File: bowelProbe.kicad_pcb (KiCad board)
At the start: 2 copper layers, 119.8 x 64.8 mm, 53 parts, among them J10 Conn_01x01, J11 Conn_01x01, J12 Conn_01x01, J13 Conn_01x01, J2 Conn_01x01, J3 Conn_01x01, J4 Conn_01x01, J5 Conn_01x01, J6 Conn_01x01, J7 Conn_01x01, J8 Conn_01x01, J9 Conn_01x01, U1 MAX038CPP, U2 OPA2134PA, U3 MCP6002-E/P, U4 TL072ACP

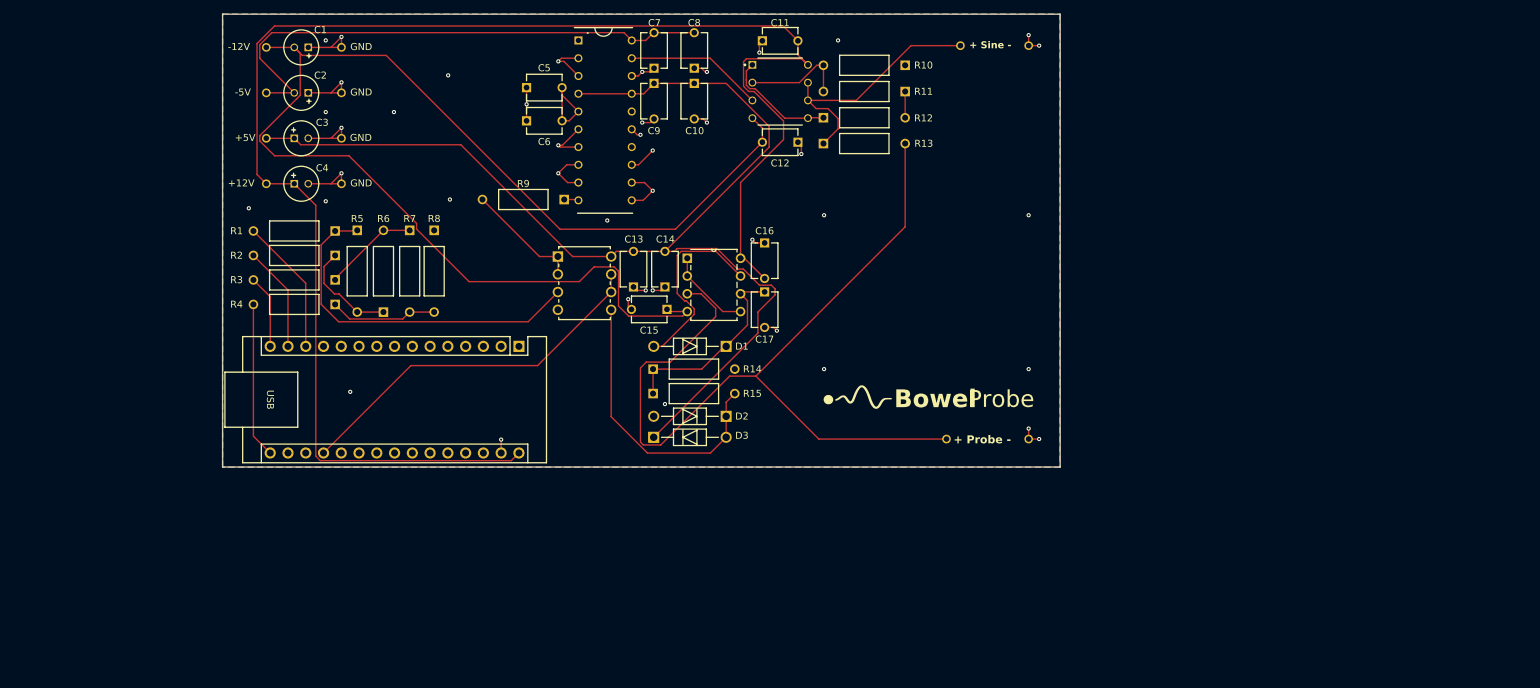
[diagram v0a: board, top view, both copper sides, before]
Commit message: Finished Electronic Schematic, Awaiting Finalizations and Review
Added many symbols, footprints, and 3d models. Organized design into functional blocks.

Still need finalized plans and footprints for "demo".

Next Steps:
 - Finalize "demo" subciruit
 - Review schematic

- Move on to layout

- Make code for full device operation
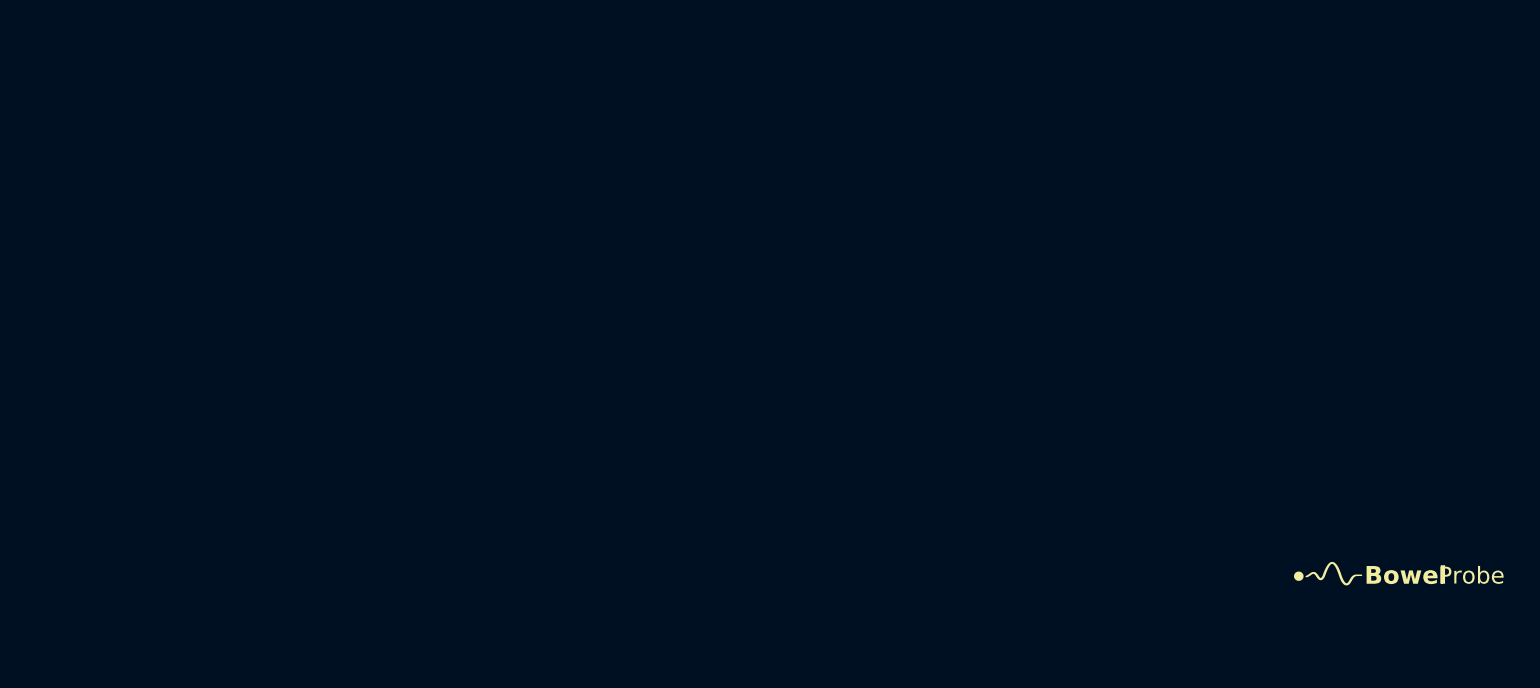
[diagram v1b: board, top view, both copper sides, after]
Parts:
- removed A1: Arduino_Nano_v2.x, Module:Arduino_Nano
- removed C1, C2, C3, C4: 10u, BowelProbe:Capacitor-10u
- removed C10, C14, C8: 1u, BowelProbe:Capacitor-10n
- removed C11, C12, C13, C15, C16, C17: 0.1u, BowelProbe:Capacitor-10n
- removed C5, C6: 10n, BowelProbe:Capacitor-10n
- removed C7, C9: 1n, BowelProbe:Capacitor-10n
- removed D1, D2, D3: DIOAD1036W78L470D235, BowelProbe:1N5817
- removed J10, J11: Conn_01x01, BowelProbe:CT3149-5
- removed J12, J13, J3, J4, J6, J8: Conn_01x01, BowelProbe:CT3149-0
- removed J2, J5, J7, J9: Conn_01x01, BowelProbe:CT3149-2
- removed R1, R11, R12, R2, R3, R4, R8: 20k, BowelProbe:Resistor-20k
- removed R10, R5, R6, R7: 10k, BowelProbe:Resistor-20k
- removed R13: 100, BowelProbe:Resistor-20k
- removed R14: 300k, BowelProbe:Resistor-20k
- removed R15: 1k, BowelProbe:Resistor-20k
- removed R9: 25k, BowelProbe:Resistor-20k
- removed U1: MAX038CPP, BowelProbe:MAX038CPP
- removed U2: OPA2134PA, BowelProbe:DIP794W45P254L959H508Q8
- removed U3: MCP6002-E/P, BowelProbe:PDIP8_300MC_MCH
- removed U4: TL072ACP, BowelProbe:P8
- moved G*** 71.8 mm to (249.1, 115.0)
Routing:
- net Net-(A1-VIN): track 225.7 -> 0.00 mm
- net Net-(J5-Pin_1): track 186.9 -> 0.00 mm
- net Net-(D3-K): track 165.5 -> 0.00 mm
- net Net-(J10-Pin_1): track 124.7 -> 0.00 mm
- net GND: track 101.9 -> 0.00 mm, vias 42 -> 0
- net Net-(J2-Pin_1): track 76.7 -> 0.00 mm
- net Net-(A1-A0): track 53.2 -> 0.00 mm
- net Net-(R1-Pad1): track 51.1 -> 0.00 mm
- net Net-(D2-K): track 41.6 -> 0.00 mm
- net Net-(J12-Pin_1): track 37.4 -> 0.00 mm
- net Net-(D1-K): track 28.0 -> 0.00 mm
- net Net-(D1-A): track 28.0 -> 0.00 mm
- net Net-(A1-D13): track 22.2 -> 0.00 mm
- net Net-(U1-OUT): track 19.7 -> 0.00 mm
- net Net-(A1-D10): track 19.6 -> 0.00 mm
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- removed copper zone on B.Cu, net GND
- removed copper zone on F.Cu, net GND
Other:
- board outline removed
- board text removed: "+ Probe -"
- board text removed: "+ Sine -"
- board text removed: "+12V"
- board text removed: "+5V"
- board text removed: "-12V"
- board text removed: "-5V"
- board text removed: "GND"

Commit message: LTspice Source Scripting
Created python script to model sine wave generator (replacement model for chip AD9833 w/o spice model). Additionally began initial pcb placement.
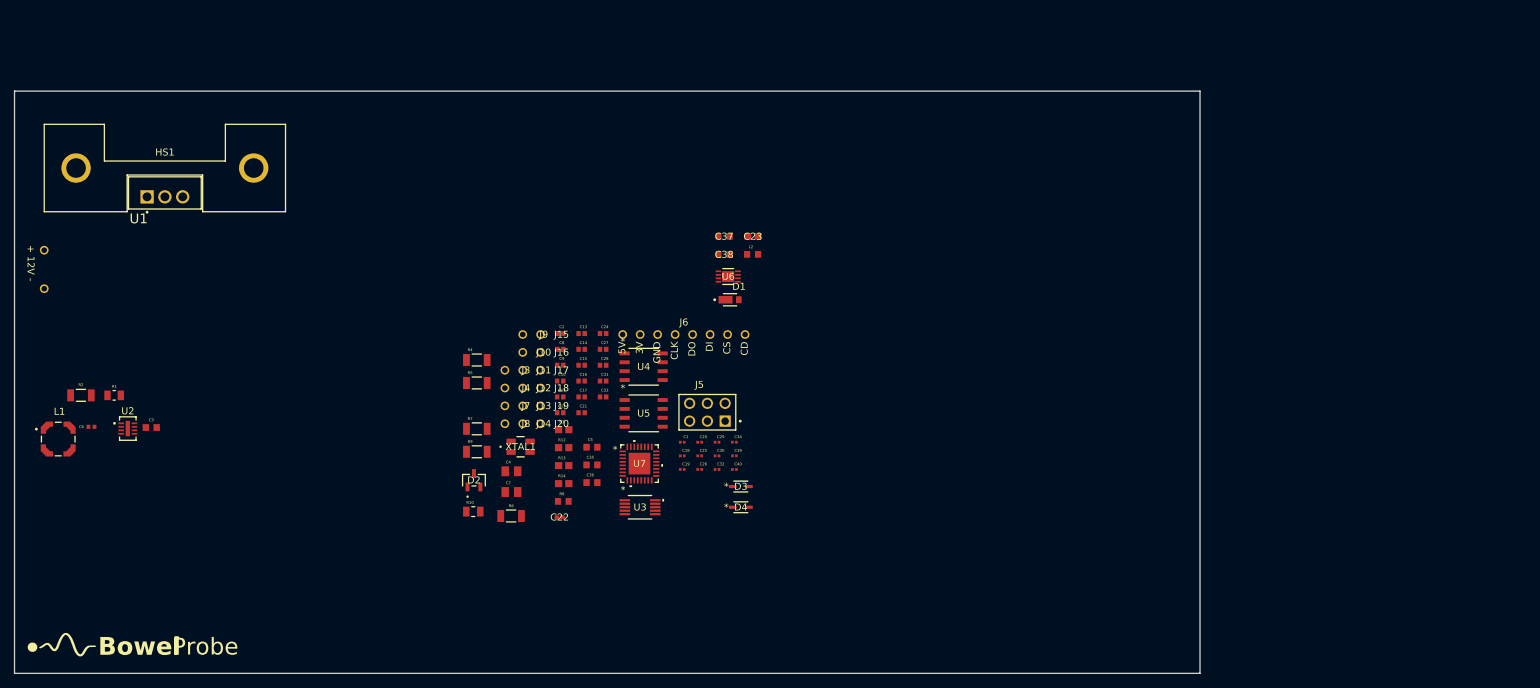
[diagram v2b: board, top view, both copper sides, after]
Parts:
- added C1: 0.1u, BowelProbe:Cap0.1uF, F.Cu at (156.7, 95.7)
- added C10: 10u, BowelProbe:Cap10uF, F.Cu at (139.3, 87.0)
- added C11: 10u, BowelProbe:Cap10uF, F.Cu at (139.3, 89.2)
- added C12: 10u, BowelProbe:Cap10uF, F.Cu at (139.3, 91.5)
- added C13: 10u, BowelProbe:Cap10uF, F.Cu at (142.3, 80.2)
- added C14: 10u, BowelProbe:Cap10uF, F.Cu at (142.3, 82.4)
- added C15: 10u, BowelProbe:Cap10uF, F.Cu at (142.3, 84.7)
- added C16: 10u, BowelProbe:Cap10uF, F.Cu at (142.3, 87.0)
- added C17: 10u, BowelProbe:Cap10uF, F.Cu at (142.3, 89.2)
- added C18: 0.1u, BowelProbe:Cap0.1uF, F.Cu at (156.7, 97.6)
- added C19: 0.1u, BowelProbe:Cap0.1uF, F.Cu at (156.7, 99.6)
- added C2: 10u, BowelProbe:Cap10uF, F.Cu at (139.3, 80.2)
- added C20: 0.1u, BowelProbe:Cap0.1uF, F.Cu at (159.2, 95.7)
- added C21: 10u, BowelProbe:Cap10uF, F.Cu at (142.3, 91.5)
- added C22: 2.2n, BowelProbe:Cap2.2nF, F.Cu at (139.2, 106.4)
- added C23: 1n, BowelProbe:Cap1nF, F.Cu at (166.8, 66.3)
- added C24: 10u, BowelProbe:Cap10uF, F.Cu at (145.4, 80.2)
- added C25: 0.1u, BowelProbe:Cap0.1uF, F.Cu at (159.2, 97.6)
- added C26: 0.1u, BowelProbe:Cap0.1uF, F.Cu at (159.2, 99.6)
- added C27: 10u, BowelProbe:Cap10uF, F.Cu at (145.4, 82.4)
- added C28: 10u, BowelProbe:Cap10uF, F.Cu at (145.4, 84.7)
- added C29: 0.1u, BowelProbe:Cap0.1uF, F.Cu at (161.7, 95.7)
- added C3: 1u, BowelProbe:Cap1uF, F.Cu at (80.8, 93.6)
- added C30: 0.1u, BowelProbe:Cap0.1uF, F.Cu at (161.7, 97.6)
- added C31: 10u, BowelProbe:Cap10uF, F.Cu at (145.4, 87.0)
- added C32: 0.1u, BowelProbe:Cap0.1uF, F.Cu at (161.7, 99.6)
- added C33: 10u, BowelProbe:Cap10uF, F.Cu at (145.4, 89.2)
- added C34: 0.1u, BowelProbe:Cap0.1uF, F.Cu at (164.2, 95.7)
- added C35: 1u, BowelProbe:Cap1uF, F.Cu at (143.8, 98.9)
- added C36: 1u, BowelProbe:Cap1uF, F.Cu at (143.8, 101.5)
- added C37: 18p, BowelProbe:Cap18pF, F.Cu at (162.7, 66.3)
- added C38: 18p, BowelProbe:Cap18pF, F.Cu at (162.7, 68.9)
- added C39: 0.1u, BowelProbe:Cap0.1uF, F.Cu at (164.2, 97.6)
- added C4: 4.7u, BowelProbe:Cap4.7uF, F.Cu at (132.3, 99.9)
- added C40: 0.1u, BowelProbe:Cap0.1uF, F.Cu at (164.2, 99.6)
- added C5: 1u, BowelProbe:Cap1uF, F.Cu at (143.8, 96.4)
- added C6: 4.7p, BowelProbe:Cap4.7pF, F.Cu at (72.2, 93.5)
- added C7: 4.7u, BowelProbe:Cap4.7uF, F.Cu at (132.3, 102.8)
- added C8: 10u, BowelProbe:Cap10uF, F.Cu at (139.3, 82.4)
- added C9: 10u, BowelProbe:Cap10uF, F.Cu at (139.3, 84.7)
- added D1: SchottkyDiode, BowelProbe:SchottkyDiode, F.Cu at (163.6, 75.3)
- added D2: DiodeLowLeak, BowelProbe:DiodeLowLeak, F.Cu at (126.9, 101.1)
- added D3: DiodeClamper, BowelProbe:DiodeClamper, F.Cu at (165.1, 102.0)
- added D4: DiodeClamper, BowelProbe:DiodeClamper, F.Cu at (165.1, 105.0)
- added HS1: Heatsink, BowelProbe:Heatsink, F.Cu at (82.8, 56.5)
- added J1: Conn_01x01, BowelProbe:CT3149-0, F.Cu at (65.5, 73.8)
- added J10: Conn_01x01, BowelProbe:CT3149-0, F.Cu at (133.9, 82.9)
- added J11: Conn_01x01, BowelProbe:CT3149-0, F.Cu at (133.9, 85.4)
- added J12: Conn_01x01, BowelProbe:CT3149-0, F.Cu at (133.9, 88.0)
- added J13: Conn_01x01, BowelProbe:CT3149-0, F.Cu at (133.9, 90.5)
- added J14: Conn_01x01, BowelProbe:CT3149-0, F.Cu at (133.9, 93.1)
- added J15: Conn_01x01, BowelProbe:CT3149-0, F.Cu at (136.5, 80.3)
- added J16: Conn_01x01, BowelProbe:CT3149-0, F.Cu at (136.5, 82.9)
- added J17: Conn_01x01, BowelProbe:CT3149-0, F.Cu at (136.5, 85.4)
- added J18: Conn_01x01, BowelProbe:CT3149-0, F.Cu at (136.5, 88.0)
- added J19: Conn_01x01, BowelProbe:CT3149-0, F.Cu at (136.5, 90.5)
- added J2: Conn_01x01, BowelProbe:CT3149-2, F.Cu at (65.5, 68.2)
- added J20: Conn_01x01, BowelProbe:CT3149-0, F.Cu at (136.5, 93.1)
- added J3: Conn_01x01, BowelProbe:CT3149-5, F.Cu at (131.4, 85.4)
- added J4: Conn_01x01, BowelProbe:CT3149-5, F.Cu at (131.4, 88.0)
- added J5: Conn_02x03_Odd_Even, BowelProbe:Dupont2x3, F.Cu at (160.3, 91.4)
- added J6: Conn_01x08, BowelProbe:microSD, F.Cu at (157.0, 80.3)
- added J7: Conn_01x01, BowelProbe:CT3149-0, F.Cu at (131.4, 90.5)
- added J8: Conn_01x01, BowelProbe:CT3149-0, F.Cu at (131.4, 93.1)
- added J9: Conn_01x01, BowelProbe:CT3149-0, F.Cu at (133.9, 80.3)
- added L1: LPD5030-472MRC, BowelProbe:InductorCoupled, F.Cu at (67.5, 95.2)
- added L2: 10u, BowelProbe:Inductor10uH, F.Cu at (166.8, 68.8)
- added R1: 71.5k, BowelProbe:Resistor71.5k, F.Cu at (75.5, 89.0)
- added R10: 1k, BowelProbe:Resistor1k, F.Cu at (126.8, 105.6)
- added R12: 10k, BowelProbe:Resistor10k, F.Cu at (139.8, 96.5)
- added R13: 10k, BowelProbe:Resistor10k, F.Cu at (139.8, 99.0)
- added R14: 10k, BowelProbe:Resistor10k, F.Cu at (139.8, 101.6)
- added R2: 1M, BowelProbe:Resistor1M, F.Cu at (70.8, 89.0)
- added R3: 10k, BowelProbe:Resistor10k, F.Cu at (139.8, 93.9)
- added R4: 6.8k, BowelProbe:Resistor6.8k, F.Cu at (127.3, 83.9)
- added R5: 6.8k, BowelProbe:Resistor6.8k, F.Cu at (127.3, 87.2)
- added R6: 30k, BowelProbe:Resistor30k, F.Cu at (132.2, 106.2)
- added R7: 1.8k, BowelProbe:Resistor1.8k, F.Cu at (127.3, 93.8)
- added R8: 100, BowelProbe:Resistor100, F.Cu at (139.7, 104.2)
- added R9: 300k, BowelProbe:Resistor300k, F.Cu at (127.3, 97.1)
- added U1: L7805CV, BowelProbe:L7805CV, F.Cu at (80.2, 60.6)
- added U2: LT8330, BowelProbe:LT8330, F.Cu at (77.5, 93.8)
- added U3: AD9833BRMZ, BowelProbe:AD9833, F.Cu at (150.7, 105.0)
- added U4: OPA2134UA/2K5, BowelProbe:OPA2134smd, F.Cu at (151.2, 84.9)
- added U5: TL072ACDR, BowelProbe:TL072smd, F.Cu at (151.2, 91.6)
- added U6: MCP6002-E/MC, BowelProbe:MCP6002smd, F.Cu at (163.3, 72.0)
- added U7: ATmega328P, BowelProbe:ATmega328P, F.Cu at (150.6, 98.8)
- added XTAL1: TSX-3225 16.0000MF09Z-AC3, BowelProbe:Crystal16MHz, F.Cu at (133.6, 96.4)
- moved G*** 181.3 mm to (68.1, 125.2)
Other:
- board outline added: 169.5 x 83.2 mm
- board text added: "+ 12V -"

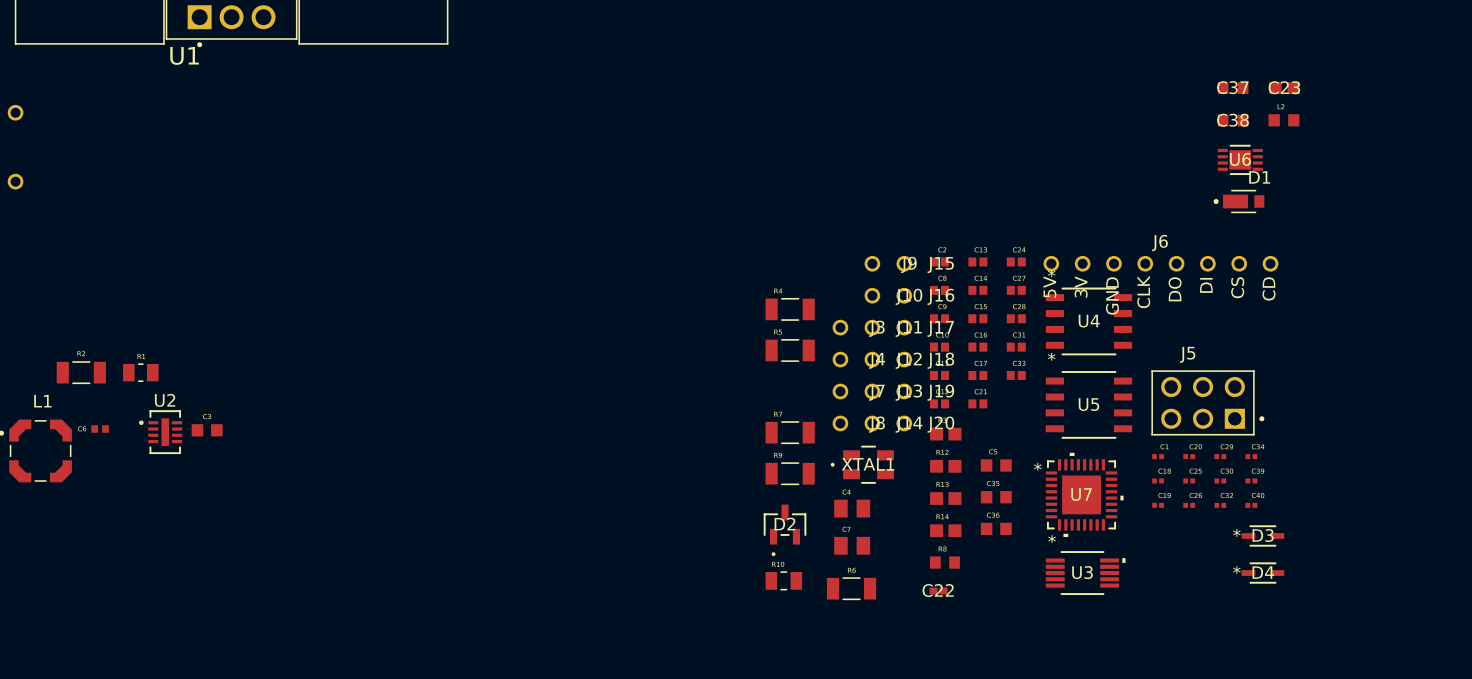
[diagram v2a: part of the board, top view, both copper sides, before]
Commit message: KiCad Updates
Added buffer after wave AD9833 sine generation and coupling capacitor (as simulated in LTspice) to address loading on filter stage. Added symbol, footprint, 3D model, and spice model in corresponding folders.

Updated BOM with this new part and updated PCB layout with buffer parts.
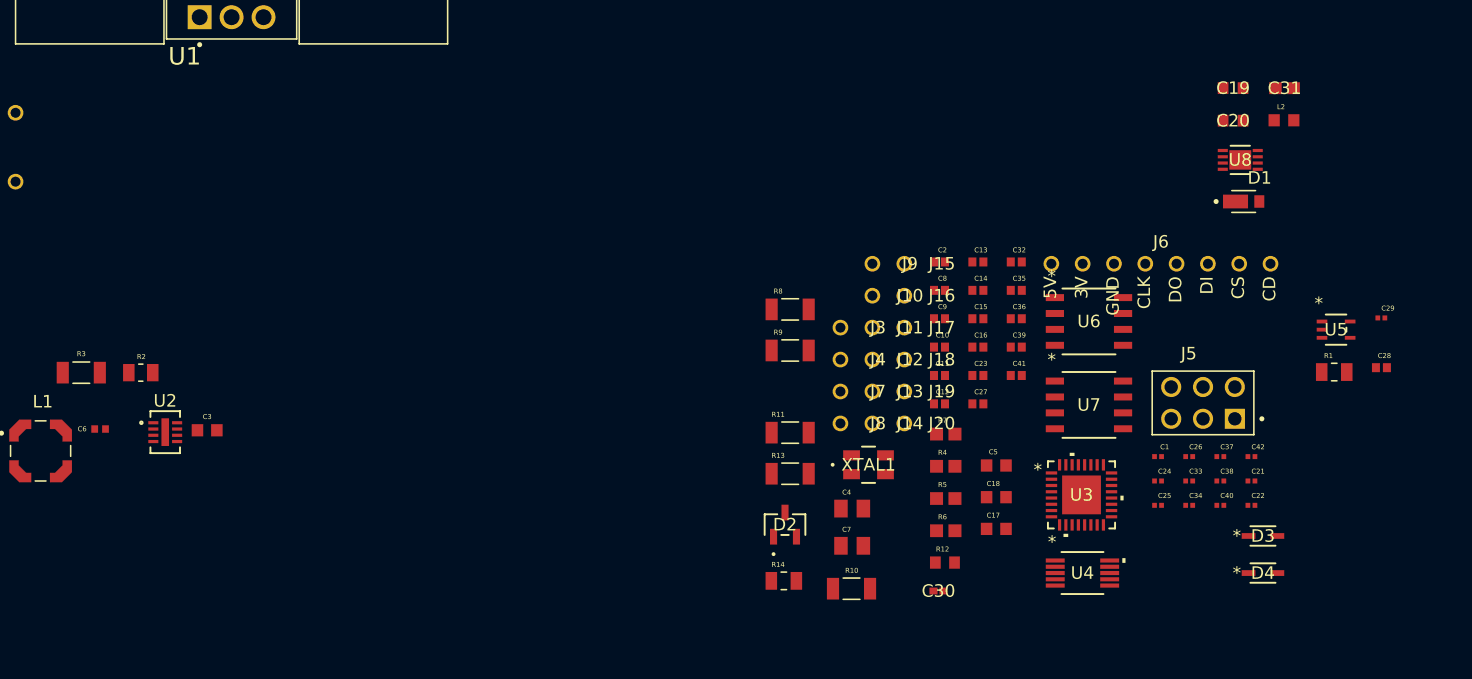
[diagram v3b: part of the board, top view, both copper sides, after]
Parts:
- added C28: 10u, BowelProbe:Cap10uF, F.Cu at (174.6, 88.6)
- added C29: 0.1u, BowelProbe:Cap0.1uF, F.Cu at (174.6, 84.6)
- added R1: 1k, BowelProbe:Resistor1k, F.Cu at (170.8, 89.0)
- added U5: Buffer, BowelProbe:Buffer, F.Cu at (170.9, 85.6)
- renumbered C36 to C17, C35 to C18, C37 to C19, C38 to C20, C39 to C21, C40 to C22, C17 to C23, C18 to C24, C19 to C25, C20 to C26, C21 to C27, C22 to C30, C23 to C31, C24 to C32, C25 to C33, C26 to C34, C27 to C35, C28 to C36, C29 to C37, C30 to C38, C31 to C39, C32 to C40, C33 to C41, C34 to C42, R6 to R10, R7 to R11, R8 to R12, R9 to R13, R10 to R14, R1 to R2, R2 to R3, R12 to R4, R13 to R5, R14 to R6, R3 to R7, R4 to R8, R5 to R9, U7 to U3, U3 to U4, U4 to U6, U5 to U7, U6 to U8
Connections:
- C1 pad 1: /+12V -> Net-(U1-INPUT)
- R8 pad 1: /Vsingen -> /Vsinbuf
- U1 pad 1: /+12V -> Net-(U1-INPUT)
- U2 pad 2: GND -> unconnected-(U2-NC-Pad2)
